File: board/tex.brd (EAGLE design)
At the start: 200 x 100 mm, 270 parts, among them K1 HLS8L-DC5V-S-C, K2 HLS8L-DC5V-S-C, K3 HLS8L-DC5V-S-C, K4 HLS8L-DC5V-S-C, Q41 FDD4141, U1 RELAY-S108T02PTH, U12 OPTO-LTV817, U13 OPTO-LTV817, U14 OPTO-LTV817, U15 OPTO-LTV817, U17 24LC32A, U18 IO-HC4051, U2 RELAY-S108T02PTH, U4 AZ23C5V1, Y1 32.768KHz

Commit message: set R and C values
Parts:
- C11, C15, C17, C18, C19, C2, C20, C21, C22, C23, C24, C25, C26, C27, C28, C29, C6, C7: value (none) -> .1u
- C13, C14: value .1u -> 10p
- D1, D10, D11, D12, D13, D14, D15, D16, D19, D2, D20, D25, D26, D27, D28, D29, D3, D30, D32, D4, D5, D6, D7, D8, D9: value (none) -> GRN
- D17, D18, D33: value (none) -> RED
- D21, D22, D23, D24, D35, D36: value (none) -> 1n4148
- D31: value (none) -> VZ=15.0
- D34: value (none) -> BLUE
- Q1, Q2, Q3, Q4: value (none) -> IRFZ44
- Q10, Q21, Q22, Q23, Q24, Q25, Q26, Q27, Q28, Q29, Q30, Q5, Q6, Q7, Q8, Q9: value (none) -> FDD4141
- Q11, Q12, Q13, Q14, Q15, Q16, Q17, Q18, Q19, Q20, Q31, Q32, Q33, Q34, Q35, Q36, Q37, Q38, Q39, Q40, Q42, Q43, Q44, Q45, Q46, Q47: value (none) -> 2N7002
- R1, R10, R11, R12, R13, R14, R15, R16, R17, R18, R2, R29, R3, R30, R31, R32, R4, R5, R58, R59, R6, R65, R66, R67, R68, R7, R8, R9: value (none) -> 1k
- R20, R21, R22, R23, R24, R27, R35, R36, R37, R38, R41, R42, R45, R46, R47, R48, R49, R50, R80, R81, R82, R83, R84, R85, R86, R88: value (none) -> 47k
- R25, R26, R60, R61, R62: value (none) -> 220
- R33, R34: value (none) -> 1
- R51: value (none) -> 10
- R64: value (none) -> 0
- R75: value (none) -> DNP
- R76, R87, R89, R90, R91, R92, R93, R94: value (none) -> 10k
- R78: value (none) -> 100

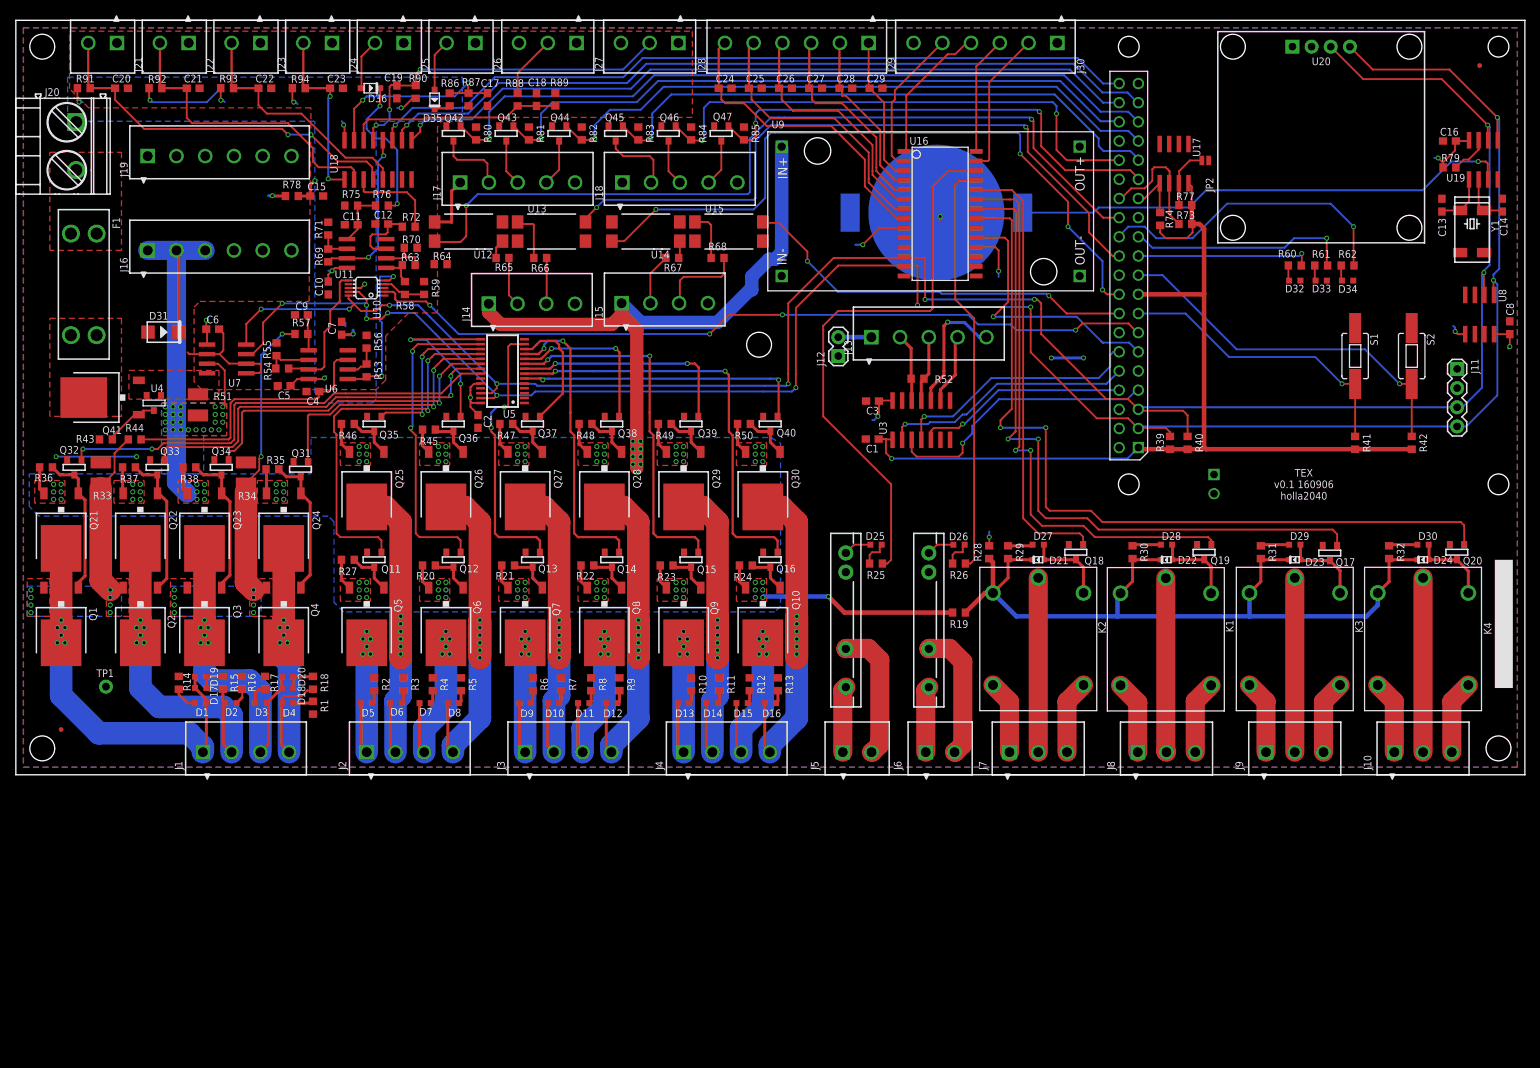
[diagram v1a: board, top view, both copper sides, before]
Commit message: changed connectors to match new lib naming
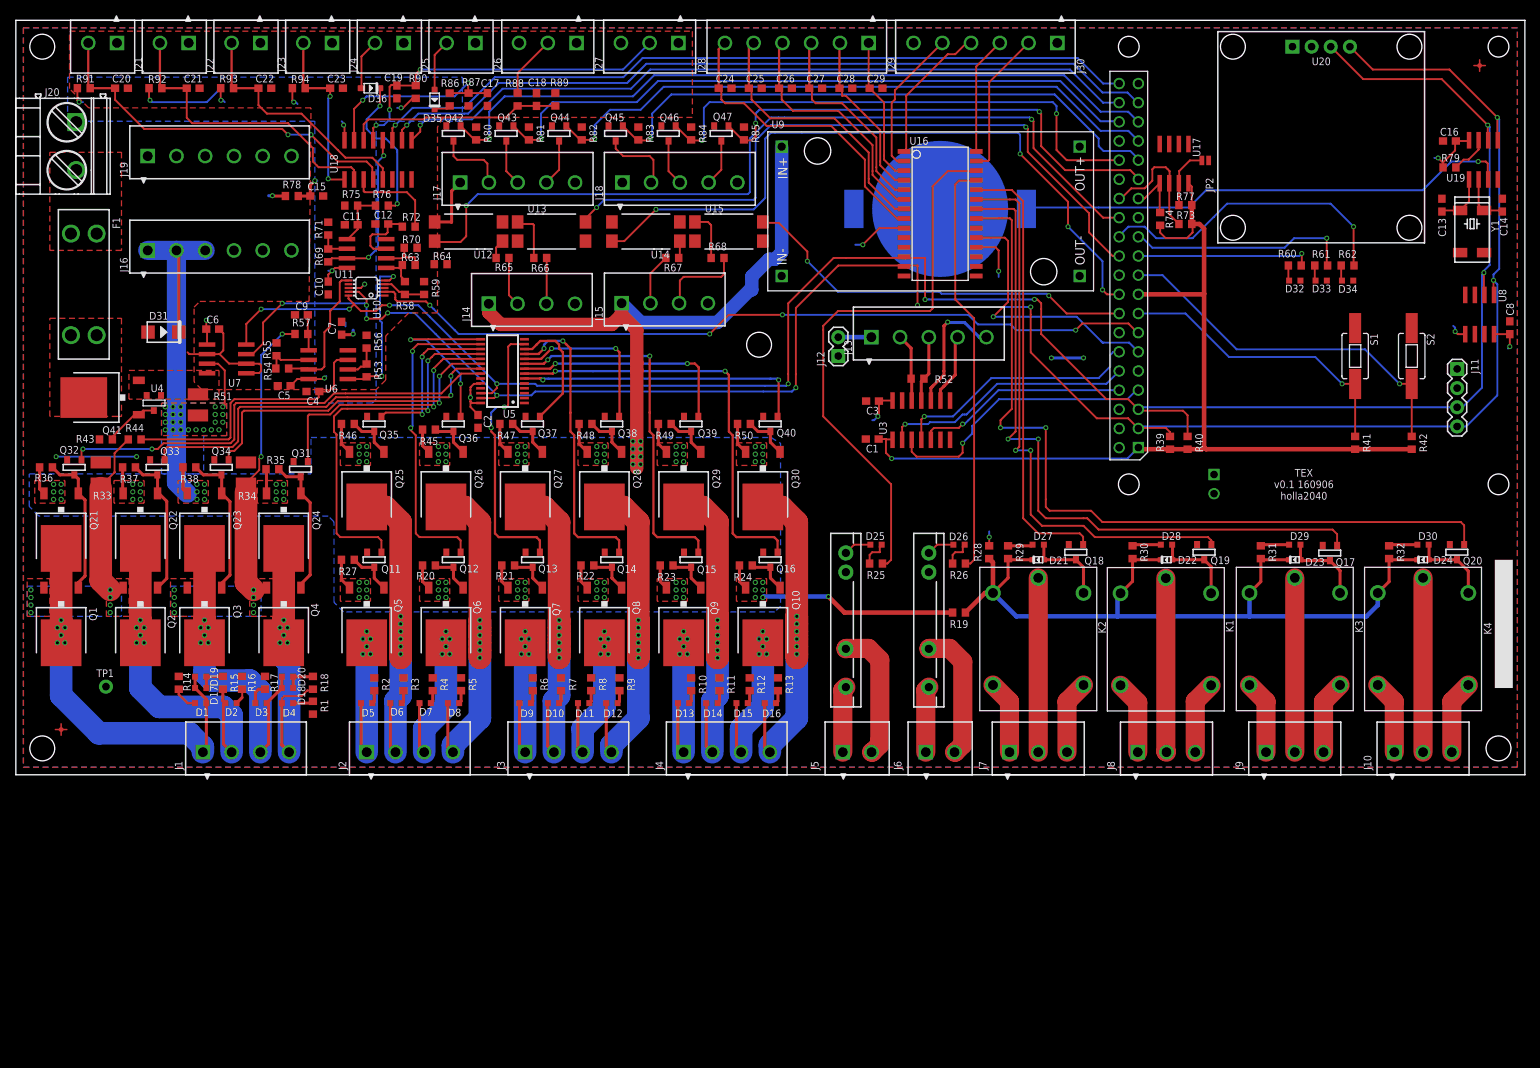
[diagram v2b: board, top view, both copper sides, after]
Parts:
- removed B100: CONN-COINBATTERYHOLDER-20MM, holla:BAT-HLD-001
- added B1: (no value), holla:BAT-HLD-001
- C13, C14: value 10p -> 12p
- R78: value 100 -> 120
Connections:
- net GND: now also B1.-; no longer B100.-
- net N$118: now also B1.+1; no longer B100.+1
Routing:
- net GND: track 41.2 -> 40.0 mm, vias 5 -> 4
- net N$118: track 66.7 -> 66.1 mm

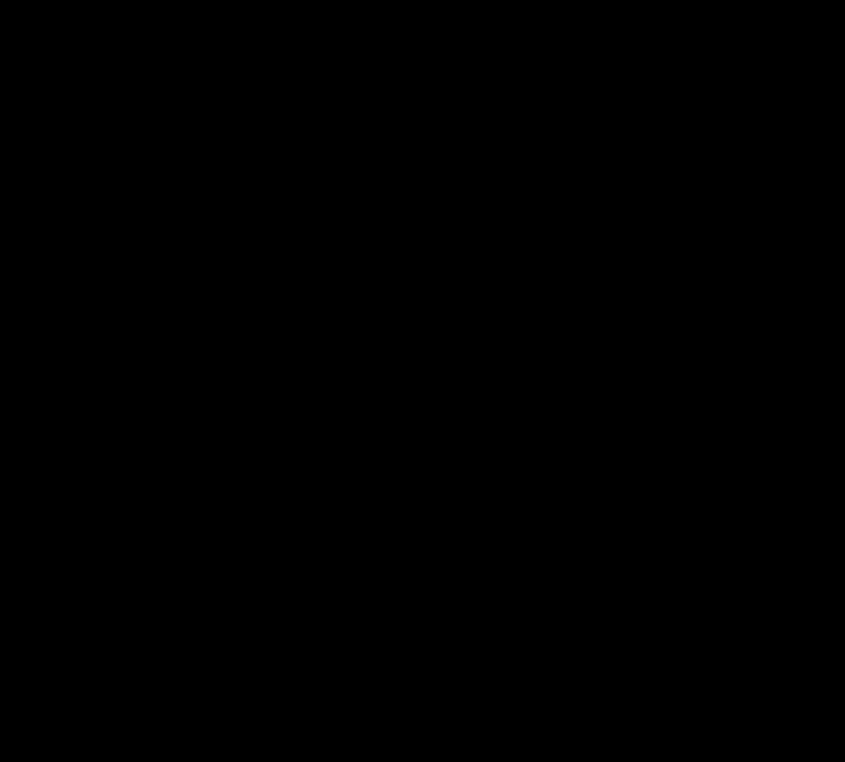
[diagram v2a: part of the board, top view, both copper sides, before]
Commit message: swapped relays for new part in holla lib
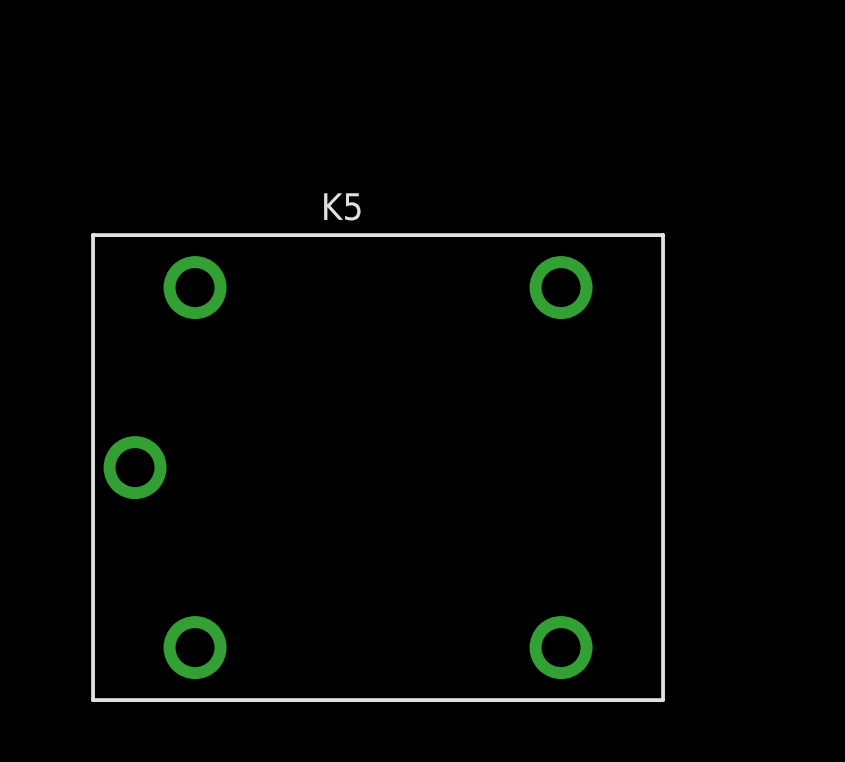
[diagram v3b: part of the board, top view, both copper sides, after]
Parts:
- added K5: (no value), holla:RELAY-SPST-19.0X15.0X15.0MM
- K1, K2, K3, K4: value HLS8L-DC5V-S-C -> (none); device holla:REY5-19.0X15.0X15.0MM -> holla:RELAY-SPST-19.0X15.0X15.0MM
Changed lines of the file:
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@@
 <attribute name="VALUE" x="77.979" y="59.5875" size="1.27" layer="27" font="vector" rot="R90"/>
 </element>
-<element name="K4" library="holla" package="REY5-19.0X15.0X15.0MM" value="HLS8L-DC5V-S-C" x="186.5" y="18" smashed="yes" rot="R270">
+<element name="K4" library="holla" package="RELAY-SPST-19.0X15.0X15.0MM" value="" x="186.5" y="18" smashed="yes" rot="R270">
 <attribute name="MPN" value="HLS8L-DC5V-S-C" x="186.5" y="18" size="1.778" layer="27" rot="R270" display="off"/>
 <attribute name="NAME" x="194.555" y="20.205" size="1.016" layer="25" ratio="21" rot="R270"/>
 <attribute name="VALUE" x="185.865" y="19.905" size="1.016" layer="27" ratio="21" rot="R270"/>
 </element>
-<element name="K3" library="holla" package="REY5-19.0X15.0X15.0MM" value="HLS8L-DC5V-S-C" x="169.5" y="18" smashed="yes" rot="R270">
+<element name="K3" library="holla" package="RELAY-SPST-19.0X15.0X15.0MM" value="" x="169.5" y="18" smashed="yes" rot="R270">
 <attribute name="MPN" value="HLS8L-DC5V-S-C" x="169.5" y="18" size="1.778" layer="27" rot="R270" display="off"/>
 <attribute name="NAME" x="177.505" y="20.455" size="1.016" layer="25" ratio="21" rot="R270"/>
 <attribute name="VALUE" x="168.865" y="19.905" size="1.016" layer="27" ratio="21" rot="R270"/>
 </element>
-<element name="K1" library="holla" package="REY5-19.0X15.0X15.0MM" value="HLS8L-DC5V-S-C" x="152.41" y="17.96" smashed="yes" rot="R270">
+<element name="K1" library="holla" package="RELAY-SPST-19.0X15.0X15.0MM" value="" x="152.41" y="17.96" smashed="yes" rot="R270">
 <attribute name="MPN" value="HLS8L-DC5V-S-C" x="152.41" y="17.96" size="1.778" layer="27" rot="R270" display="off"/>
 <attribute name="NAME" x="160.365" y="20.515" size="1.016" layer="25" ratio="21" rot="R270"/>
 <attribute name="VALUE" x="151.775" y="19.865" size="1.016" layer="27" ratio="21" rot="R270"/>
 </element>
-<element name="K2" library="holla" package="REY5-19.0X15.0X15.0MM" value="HLS8L-DC5V-S-C" x="135.5" y="18" smashed="yes" rot="R270">
+<element name="K2" library="holla" package="RELAY-SPST-19.0X15.0X15.0MM" value="" x="135.5" y="18" smashed="yes" rot="R270">
 <attribute name="MPN" value="HLS8L-DC5V-S-C" x="135.5" y="18" size="1.778" layer="27" rot="R270" display="off"/>
 <attribute name="NAME" x="143.455" y="20.355" size="1.016" layer="25" ratio="21" rot="R270"/>
@@
 </element>
 <element name="B1" library="holla" package="BAT-HLD-001" value="" x="122.5" y="75" rot="MR0"/>
+<element name="K5" library="holla" package="RELAY-SPST-19.0X15.0X15.0MM" value="" x="10.5" y="-29"/>
 </elements>
 <signals>

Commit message: added descriptions to all circuit elements, generated update schematic
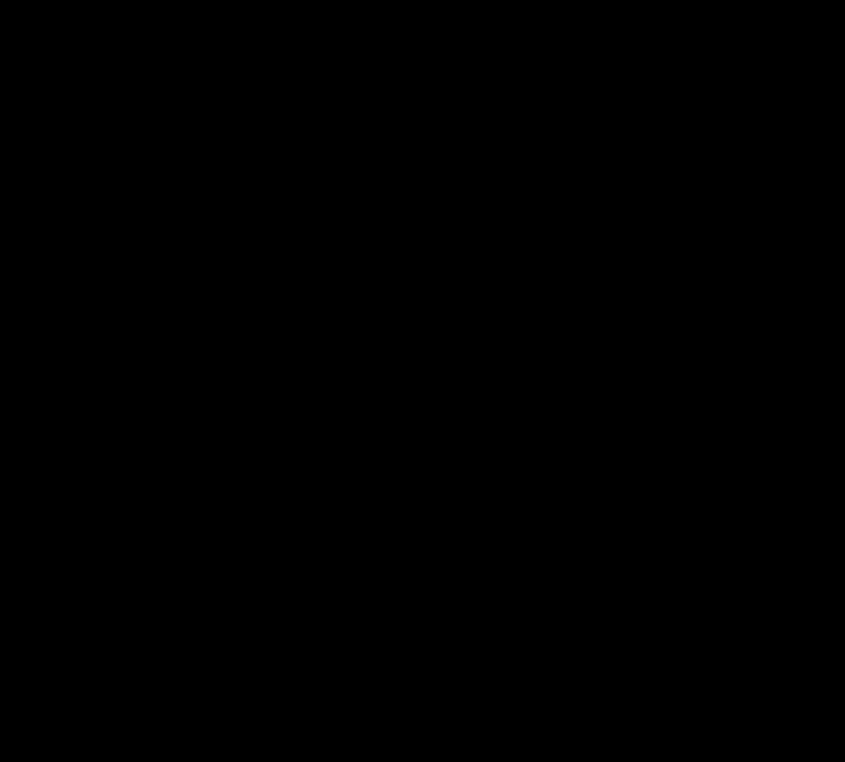
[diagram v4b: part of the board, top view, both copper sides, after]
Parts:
- removed K5: (no value), holla:RELAY-SPST-19.0X15.0X15.0MM
- U1, U2: value RELAY-S108T02PTH -> (none)
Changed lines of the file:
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@@
 <attribute name="VALUE" x="134.865" y="28.595" size="1.27" layer="27"/>
 </element>
-<element name="U2" library="holla" package="RELAY-S108T02" value="RELAY-S108T02PTH" x="121" y="20.5" smashed="yes" rot="R90"/>
-<element name="U1" library="holla" package="RELAY-S108T02" value="RELAY-S108T02PTH" x="110" y="20.5" smashed="yes" rot="R90"/>
+<element name="U2" library="holla" package="RELAY-S108T02" value="" x="121" y="20.5" smashed="yes" rot="R90"/>
+<element name="U1" library="holla" package="RELAY-S108T02" value="" x="110" y="20.5" smashed="yes" rot="R90"/>
 <element name="J6" library="holla" package="CONN-3.81MM-KF2EDG-2" value="" x="122.5" y="3" smashed="yes">
 <attribute name="NAME" x="117.381" y="0.6575" size="1.016" layer="25" font="vector" ratio="21" rot="R90"/>
@@
 </element>
 <element name="B1" library="holla" package="BAT-HLD-001" value="" x="122.5" y="75" rot="MR0"/>
-<element name="K5" library="holla" package="RELAY-SPST-19.0X15.0X15.0MM" value="" x="10.5" y="-29"/>
 </elements>
 <signals>

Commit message: added part number
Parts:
- U10: value (none) -> ADS1x15
- U11, U6: value (none) -> DUALOPAMP
- U16: value (none) -> MCP23017
- U19: value (none) -> MCP7940N
- U3: value (none) -> MAX13433E
- U5: value (none) -> PCA9685
- U7: value (none) -> INA219
- U8: value (none) -> LM75
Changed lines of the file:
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@@
 <attribute name="VALUE" x="188.936" y="75.683" size="1.016" layer="27" ratio="21" rot="R270"/>
 </element>
-<element name="U10" library="holla" package="MSOP10_0.5" value="" x="46.482" y="64.516" smashed="yes" rot="R90">
+<element name="U10" library="holla" package="MSOP10_0.5" value="ADS1x15" x="46.482" y="64.516" smashed="yes" rot="R90">
 <attribute name="NAME" x="47.316" y="62.922" size="1.016" layer="25" ratio="21" rot="R270"/>
 <attribute name="VALUE" x="49.022" y="67.818" size="1.27" layer="27" ratio="10" rot="R180"/>
@@
 <attribute name="DESC" value="16V Y5V -20%,+80%" x="198" y="59.25" size="1.778" layer="27" rot="R90" display="off"/>
 </element>
-<element name="U8" library="holla" package="SO08" value="" x="194" y="61" smashed="yes" rot="R180">
+<element name="U8" library="holla" package="SO08" value="LM75" x="194" y="61" smashed="yes" rot="R180">
 <attribute name="NAME" x="196.517" y="64.37" size="1.016" layer="25" ratio="21" rot="R270"/>
 <attribute name="VALUE" x="191.333" y="61" size="1.016" layer="27" ratio="21" rot="R270" align="top-center"/>
@@
 <attribute name="DESC" value="5%" x="176.5" y="67.5" size="1.778" layer="27" display="off"/>
 </element>
-<element name="U5" library="holla" package="TSSOP28" value="" x="64.5" y="53.5" smashed="yes" rot="R90">
+<element name="U5" library="holla" package="TSSOP28" value="PCA9685" x="64.5" y="53.5" smashed="yes" rot="R90">
 <attribute name="NAME" x="66.256" y="48.346" size="1.016" layer="25" ratio="21" rot="R180"/>
 </element>
@@
 <attribute name="DESC" value="5%" x="34.544" y="56.388" size="1.778" layer="27" rot="R270" display="off"/>
 </element>
-<element name="U6" library="holla" package="SO08" value="" x="41.402" y="54.356" smashed="yes" rot="R90">
+<element name="U6" library="holla" package="SO08" value="DUALOPAMP" x="41.402" y="54.356" smashed="yes" rot="R90">
 <attribute name="NAME" x="42.672" y="51.689" size="1.016" layer="25" ratio="21" rot="R180"/>
 <attribute name="VALUE" x="41.402" y="57.023" size="1.016" layer="27" ratio="21" rot="R180" align="top-center"/>
@@
 <attribute name="DESC" value="5%" x="125" y="21.5" size="1.778" layer="27" rot="R180" display="off"/>
 </element>
-<element name="U16" library="holla" package="SO28W" value="" x="122.5" y="75" smashed="yes" rot="R270">
+<element name="U16" library="holla" package="SO28W" value="MCP23017" x="122.5" y="75" smashed="yes" rot="R270">
 <attribute name="MF" value="MICROCHIP" x="122.5" y="75" size="1.778" layer="27" rot="R270" display="off"/>
 <attribute name="MPN" value="MCP23017-E/SO" x="122.5" y="75" size="1.778" layer="27" rot="R270" display="off"/>
@@
 <attribute name="DESC" value="5%" x="60" y="89.5" size="1.778" layer="27" rot="R90" display="off"/>
 </element>
-<element name="U7" library="holla" package="SOIC8" value="" x="27.94" y="55.118" smashed="yes" rot="R90">
+<element name="U7" library="holla" package="SOIC8" value="INA219" x="27.94" y="55.118" smashed="yes" rot="R90">
 <attribute name="NAME" x="29.845" y="52.451" size="1.016" layer="25" ratio="21" rot="R180"/>
 <attribute name="VALUE" x="29.845" y="59.055" size="1.27" layer="27" rot="R180"/>
@@
 <attribute name="VALUE" x="169" y="92" size="1.27" layer="27"/>
 </element>
-<element name="U3" library="holla" package="SO14" value="" x="120" y="47" smashed="yes">
+<element name="U3" library="holla" package="SO14" value="MAX13433E" x="120" y="47" smashed="yes">
 <attribute name="NAME" x="115.428" y="45.095" size="1.016" layer="25" ratio="21" rot="R90"/>
 <attribute name="VALUE" x="125.842" y="45.095" size="1.27" layer="27" rot="R90"/>
@@
 <attribute name="DESC" value="5%" x="41.402" y="72.39" size="1.778" layer="27" rot="R270" display="off"/>
 </element>
-<element name="U11" library="holla" package="SO08" value="" x="46.482" y="69.088" smashed="yes" rot="R90">
+<element name="U11" library="holla" package="SO08" value="DUALOPAMP" x="46.482" y="69.088" smashed="yes" rot="R90">
 <attribute name="NAME" x="42.248" y="65.829" size="1.016" layer="25" ratio="21"/>
 <attribute name="VALUE" x="46.482" y="71.755" size="1.016" layer="27" ratio="21" rot="R180" align="top-center"/>
@@
 <attribute name="DESC" value="5%" x="11.938" y="44.45" size="1.778" layer="27" rot="R180" display="off"/>
 </element>
-<element name="U19" library="holla" package="SO08" value="" x="194.5" y="81.5" smashed="yes">
+<element name="U19" library="holla" package="SO08" value="MCP7940N" x="194.5" y="81.5" smashed="yes">
 <attribute name="NAME" x="189.58" y="78.617" size="1.016" layer="25" ratio="21"/>
 <attribute name="VALUE" x="197.167" y="81.5" size="1.016" layer="27" ratio="21" rot="R90" align="top-center"/>
